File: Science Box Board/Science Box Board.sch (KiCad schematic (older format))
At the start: 40 parts, among them U10 LB1930MC, U11 Molex_SL-10, U12 Molex_SL_2, U13 Molex_SL_5, U3 5V OKI, U4 OPA320, U5 OPA320, U6 5V OKI, U7 TM4C129E_Launchpad_Full, U8 BA00DD0WHFP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

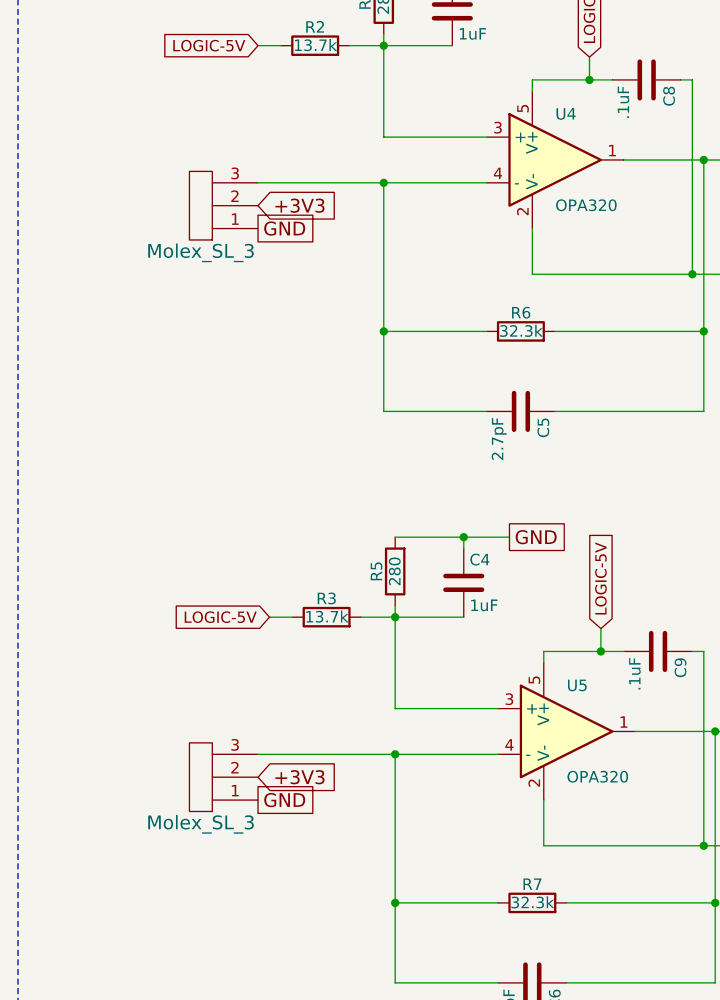
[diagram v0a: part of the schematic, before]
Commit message: Added new Ba00dwop footrpint and switched SL2 to SL3 for Photodiode
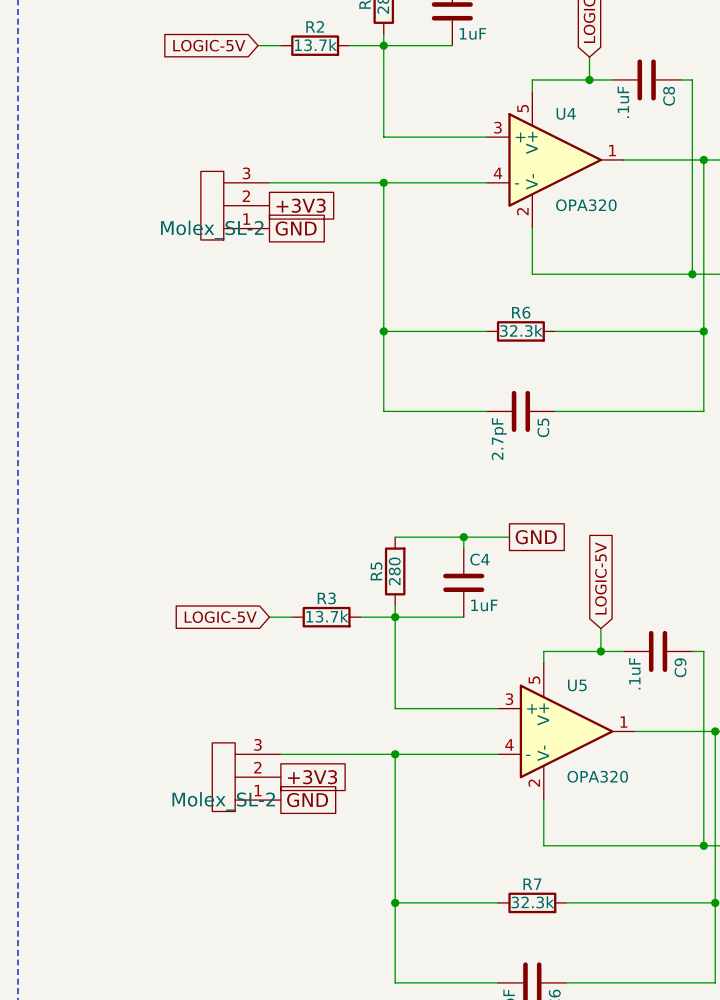
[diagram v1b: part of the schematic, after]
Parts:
- removed Conn? (x2): Molex_SL_3, symbol Molex_SL_3
- added U1, U2: Molex_SL-2, MRDT_Connectors:MOLEX_SL_2_Horizontal, symbol Molex_SL_3
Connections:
- net +3V3: now also U1.2, U2.2
- net GND: now also U1.1, U2.1
- net at C5.2, R6.1, U4.4 (-): now also U1.3
- net at C6.2, R7.1, U5.4 (-): now also U2.3
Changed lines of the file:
@@
 	1    0    0    -1
+$EndComp
+$Comp
+L Molex_SL_3 U1
+U 1 1 5AB1FE22
+P 3400 5150
+F 0 "U1" H 3450 5100 60  0001 C CNN
+F 1 "Molex_SL-2" H 3450 5400 60  0000 C CNN
+F 2 "MRDT_Connectors:MOLEX_SL_2_Horizontal" H 3400 5050 60  0001 C CNN
+F 3 "" H 3400 5050 60  0001 C CNN
+	1    3400 5150
+	-1   0    0    1
 $EndComp
 Text GLabel 3550 4600 0    49   Input ~ 0
@@
 	1    0    0    -1
 $EndComp
+$Comp
+L Molex_SL_3 U2
+U 1 1 5AB21C1D
+P 3450 7650
+F 0 "U2" H 3500 7600 60  0001 C CNN
+F 1 "Molex_SL-2" H 3500 7900 60  0000 C CNN
+F 2 "MRDT_Connectors:MOLEX_SL_2_Horizontal" H 3450 7550 60  0001 C CNN
+F 3 "" H 3450 7550 60  0001 C CNN
+	1    3450 7650
+	-1   0    0    1
+$EndComp
 Text GLabel 3600 7100 0    49   Input ~ 0
 LOGIC-5V
@@
 	2500 4150 7150 4150
 Wire Wire Line
-	3550 5200 4550 5200
+	3600 5200 4550 5200
 Wire Wire Line
 	3550 4600 3650 4600
@@
 Connection ~ 5000 4750
 Wire Wire Line
-	3550 7700 4600 7700
+	3650 7700 4600 7700
 Wire Wire Line
 	3600 7100 3700 7100
@@
 Text GLabel 5700 3100 0    60   UnSpc ~ 0
 GND
-Text GLabel 3550 5400 2    60   UnSpc ~ 0
-GND
-Text GLabel 3550 7900 2    60   UnSpc ~ 0
+Text GLabel 3600 5400 2    60   UnSpc ~ 0
+GND
+Text GLabel 3650 7900 2    60   UnSpc ~ 0
 GND
 Connection ~ 5500 8100
@@
 Text GLabel 9500 5550 2    49   Output ~ 0
 LOGIC-5V
-$Comp
-L Molex_SL_3 Conn?
-U 1 1 5AD93F33
-P 3350 5150
-F 0 "Conn?" H 3400 5100 60  0001 C CNN
-F 1 "Molex_SL_3" H 3400 5500 60  0000 C CNN
-F 2 "" H 3350 5150 60  0001 C CNN
-F 3 "" H 3350 5150 60  0001 C CNN
-	1    3350 5150
-	-1   0    0    1
-$EndComp
-Text GLabel 3550 5300 2    60   Input ~ 0
+Text GLabel 3600 5300 2    60   UnSpc ~ 0
 +3V3
-$Comp
-L Molex_SL_3 Conn?
-U 1 1 5AD94E13
-P 3350 7650
-F 0 "Conn?" H 3400 7600 60  0001 C CNN
-F 1 "Molex_SL_3" H 3400 8000 60  0000 C CNN
-F 2 "" H 3350 7650 60  0001 C CNN
-F 3 "" H 3350 7650 60  0001 C CNN
-	1    3350 7650
-	-1   0    0    1
-$EndComp
-Text GLabel 3550 7800 2    60   Input ~ 0
+Text GLabel 3650 7800 2    60   UnSpc ~ 0
 +3V3
 $EndSCHEMATC
